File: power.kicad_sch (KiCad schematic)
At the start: 32 parts, among them SW1 PCM12SMTR

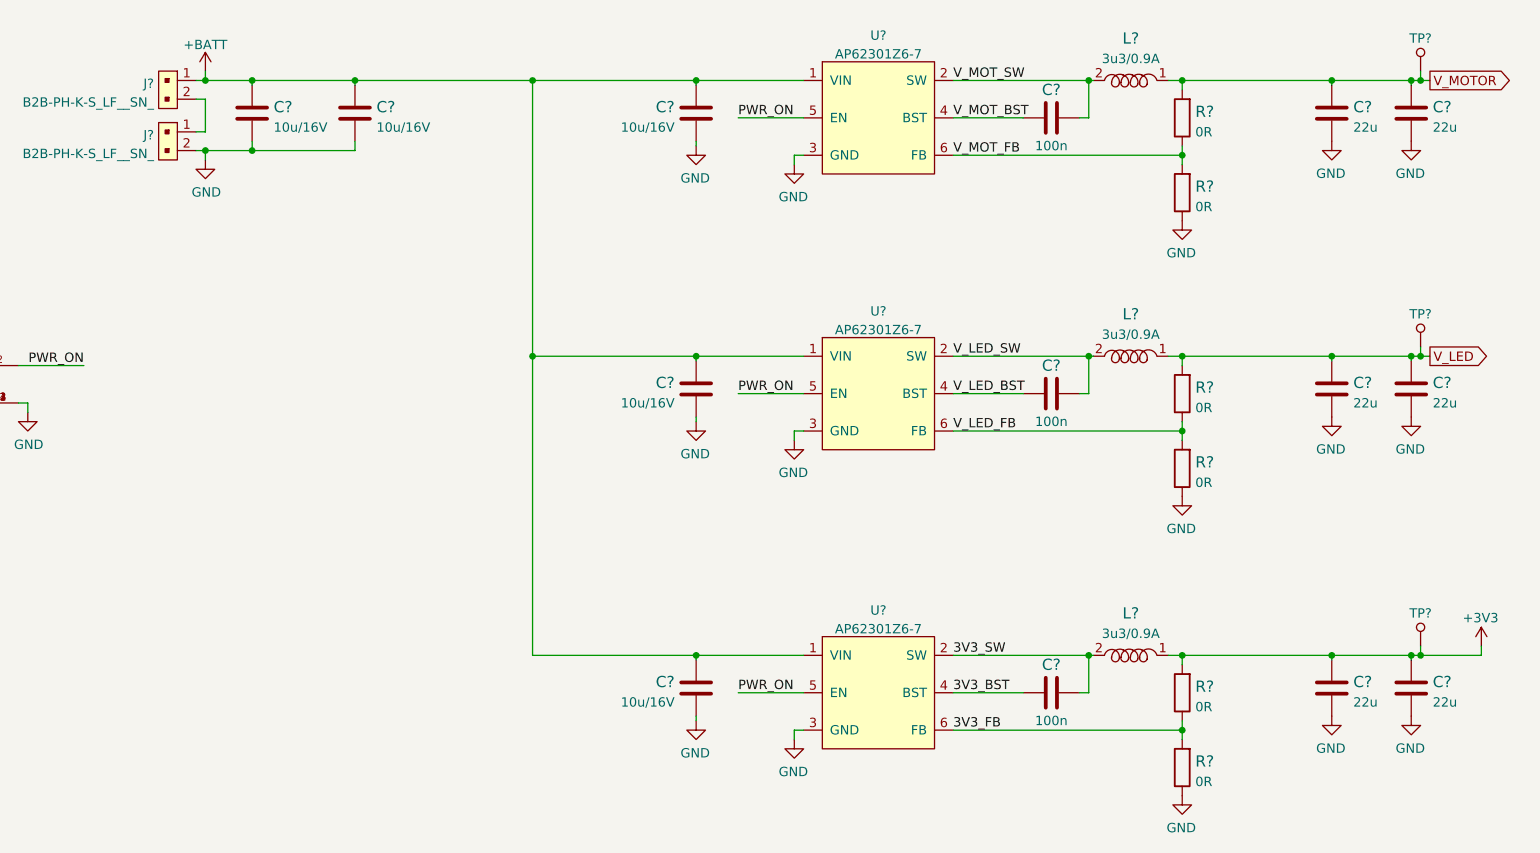
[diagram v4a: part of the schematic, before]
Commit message: Add DCDC converters
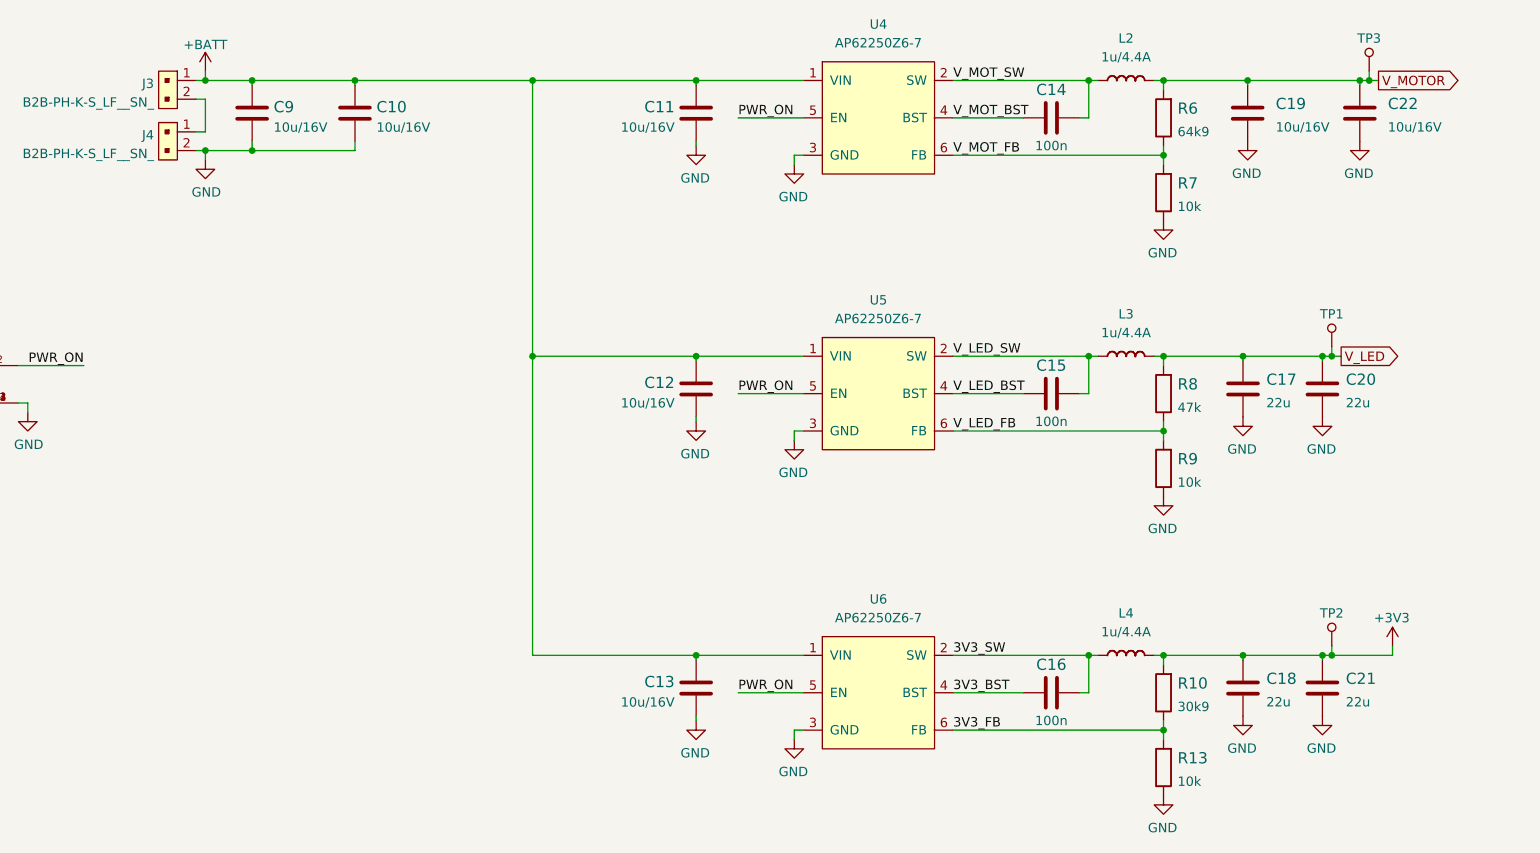
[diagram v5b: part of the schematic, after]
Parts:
- removed C? (x6): C_22u_0805_10V, antmicro-footprints:0805-cap, symbol antmicroCapacitorsmisc:C_22u_0805_10V
- removed L? (x3): MLP2012S3R3MT, antmicro-footprints:0805-res, symbol antmicroFixedInductors:MLP2012S3R3MT
- removed R? (x6): R_0R_0402, antmicro-footprints:0402-res, symbol antmicroResistors0402:R_0R_0402
- removed U? (x3): AP62301Z6-7, antmicro-footprints:SOT-563, symbol antmicroDCDCConverters:AP62301Z6-7
- added C17, C18, C20, C21: C_22u_0402, antmicro-footprints:0402-cap, symbol antmicroCapacitors0402:C_22u_0402
- added C19, C22: C_10u_16V_0603, antmicro-footprints:0603-cap, symbol antmicroCapacitors0603:C_10u_16V_0603
- added L2, L3, L4: 74479276210C, antmicro-footprints:L_0806_2016Metric, symbol antmicroFixedInductors:74479276210C
- added R10: R_30k9_0402, antmicro-footprints:0402-res, symbol antmicroResistors0402:R_30k9_0402
- added R13, R7, R9: R_10k_0402, antmicro-footprints:0402-res, symbol antmicroResistors0402:R_10k_0402
- added R6: R_64k9_0402, antmicro-footprints:0402-res, symbol antmicroResistors0402:R_64k9_0402
- added R8: R_47k_0402, antmicro-footprints:0402-res, symbol antmicroResistors0402:R_47k_0402
- added U4, U5, U6: AP62250Z6-7, antmicro-footprints:SOT-563, symbol antmicroDCDCConverters:AP62250Z6-7
- gave numbers to parts that had none: 13
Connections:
- net +3V3: now also C18.1, C21.1, L4.2 (P), R10.2
- net +BATT: now also U4.1 (VIN), U5.1 (VIN), U6.1 (VIN)
- net 3V3_BST: now also U6.4 (BST)
- net 3V3_FB: now also R10.1, R13.2, U6.6 (FB)
- net 3V3_SW: now also L4.1 (P), U6.2 (SW)
- net GND: now also C17.2, C18.2, C19.2, C20.2, C21.2, C22.2, R13.1, R7.1, R9.1, U4.3 (GND), U5.3 (GND), U6.3 (GND)
- net PWR_ON: now also U4.5 (EN), U5.5 (EN), U6.5 (EN)
- net V_LED: now also C17.1, C20.1, L3.2 (P), R8.2
- net V_LED_BST: now also U5.4 (BST)
- net V_LED_FB: now also R8.1, R9.2, U5.6 (FB)
- net V_LED_SW: now also L3.1 (P), U5.2 (SW)
- net V_MOTOR: now also C19.1, C22.1, L2.2 (P), R6.2
- net V_MOT_BST: now also U4.4 (BST)
- net V_MOT_FB: now also R6.1, R7.2, U4.6 (FB)
- net V_MOT_SW: now also L2.1 (P), U4.2 (SW)
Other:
- moved on the sheet: TP1, TP2, TP3

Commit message: Add note to the voltages
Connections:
- net V_LED renamed V_LED_RGB
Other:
- note added: "3.3V @2.5A"
- note added: "4.5V @2.5A"
- note added: "6V @2.5A"
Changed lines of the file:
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@@
     (stroke (width 0) (type default) (color 0 0 0 0))
+  )
+  (text "3.3V @2.5A" (at 262.255 151.13 0)
+    (effects (font (size 1.27 1.27)) (justify left bottom))
+  )
+  (text "4.5V @2.5A" (at 257.175 106.045 0)
+    (effects (font (size 1.27 1.27)) (justify left bottom))
+  )
+  (text "6V @2.5A" (at 261.62 68.58 0)
+    (effects (font (size 1.27 1.27)) (justify left bottom))
   )
   (label "V_LED_FB" (at 203.2 118.11 0)
@@
     (effects (font (size 1.27 1.27)) (justify left bottom))
   )
-  (global_label "V_LED" (shape output) (at 255.905 107.95 0) (fields_autoplaced)
+  (global_label "V_LED_RGB" (shape output) (at 255.905 107.95 0) (fields_autoplaced)
     (effects (font (size 1.27 1.27)) (justify left))
-    (property "Intersheet References" "${INTERSHEET_REFS}" (id 0) (at 263.7325 107.8706 0)
+    (property "Intersheet References" "${INTERSHEET_REFS}" (id 0) (at 268.5102 107.8706 0)
       (effects (font (size 1.27 1.27)) (justify left))
     )

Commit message: Loclib, cleanup
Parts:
- C10, C11, C12, C13, C19, C22, C9: footprint antmicro-footprints:0603-cap -> synermycha-electronics-footprints:0603-cap; symbol antmicroCapacitors0603:C_10u_16V_0603 -> synermycha-electronics:C_10u_16V_0603
- C14, C15, C16: footprint antmicro-footprints:0402-cap -> synermycha-electronics-footprints:0402-cap; symbol antmicroCapacitors0402:C_100n_0402 -> synermycha-electronics:C_100n_0402
- C17, C18, C20, C21: footprint antmicro-footprints:0402-cap -> synermycha-electronics-footprints:0402-cap; symbol antmicroCapacitors0402:C_22u_0402 -> synermycha-electronics:C_22u_0402
- J3, J4: footprint antmicro-footprints:PinHeader_1x2_P2mm_Drill1mm -> synermycha-electronics-footprints:PinHeader_1x2_P2mm_Drill1mm; symbol antmicroRectangularConnectorsHeadersMalePins:B2B-PH-K-S_LF__SN_ -> synermycha-electronics:B2B-PH-K-S_LF__SN_
- L2, L3, L4: footprint antmicro-footprints:L_0806_2016Metric -> synermycha-electronics-footprints:L_0806_2016Metric; symbol antmicroFixedInductors:74479276210C -> synermycha-electronics:74479276210C
- R10: footprint antmicro-footprints:0402-res -> synermycha-electronics-footprints:0402-res; symbol antmicroResistors0402:R_30k9_0402 -> synermycha-electronics:R_30k9_0402
- R13, R7, R9: footprint antmicro-footprints:0402-res -> synermycha-electronics-footprints:0402-res; symbol antmicroResistors0402:R_10k_0402 -> synermycha-electronics:R_10k_0402
- R6: footprint antmicro-footprints:0402-res -> synermycha-electronics-footprints:0402-res; symbol antmicroResistors0402:R_64k9_0402 -> synermycha-electronics:R_64k9_0402
- R8: footprint antmicro-footprints:0402-res -> synermycha-electronics-footprints:0402-res; symbol antmicroResistors0402:R_47k_0402 -> synermycha-electronics:R_47k_0402
- SW1: footprint antmicro-footprints:PCM12SMTR -> synermycha-electronics-footprints:PCM12SMTR; symbol antmicroSlideSwitches:PCM12SMTR -> synermycha-electronics:PCM12SMTR
- TP1, TP2, TP3: footprint antmicro-footprints:Testpoint_smd_0_75mm -> synermycha-electronics-footprints:Testpoint_smd_0_75mm; symbol antmicroTestPoints:TP_SMD_0_75MM -> synermycha-electronics:TP_SMD_0_75MM
- U4, U5, U6: footprint antmicro-footprints:SOT-563 -> synermycha-electronics-footprints:SOT-563; symbol antmicroDCDCConverters:AP62250Z6-7 -> synermycha-electronics:AP62250Z6-7
